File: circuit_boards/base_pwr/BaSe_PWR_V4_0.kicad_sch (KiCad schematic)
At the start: 106 parts, among them J1 12VDC In, J1 USB_C_Receptacle, J10 Conn_01x04_Socket, J11 MOTOR, J3 USB3_A, J3 USB_B_Micro, J4 Conn_01x07_Pin, J5 Conn_02x06_Odd_Even, J7 Conn_02x06_Odd_Even, J7 USB3_B_Micro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

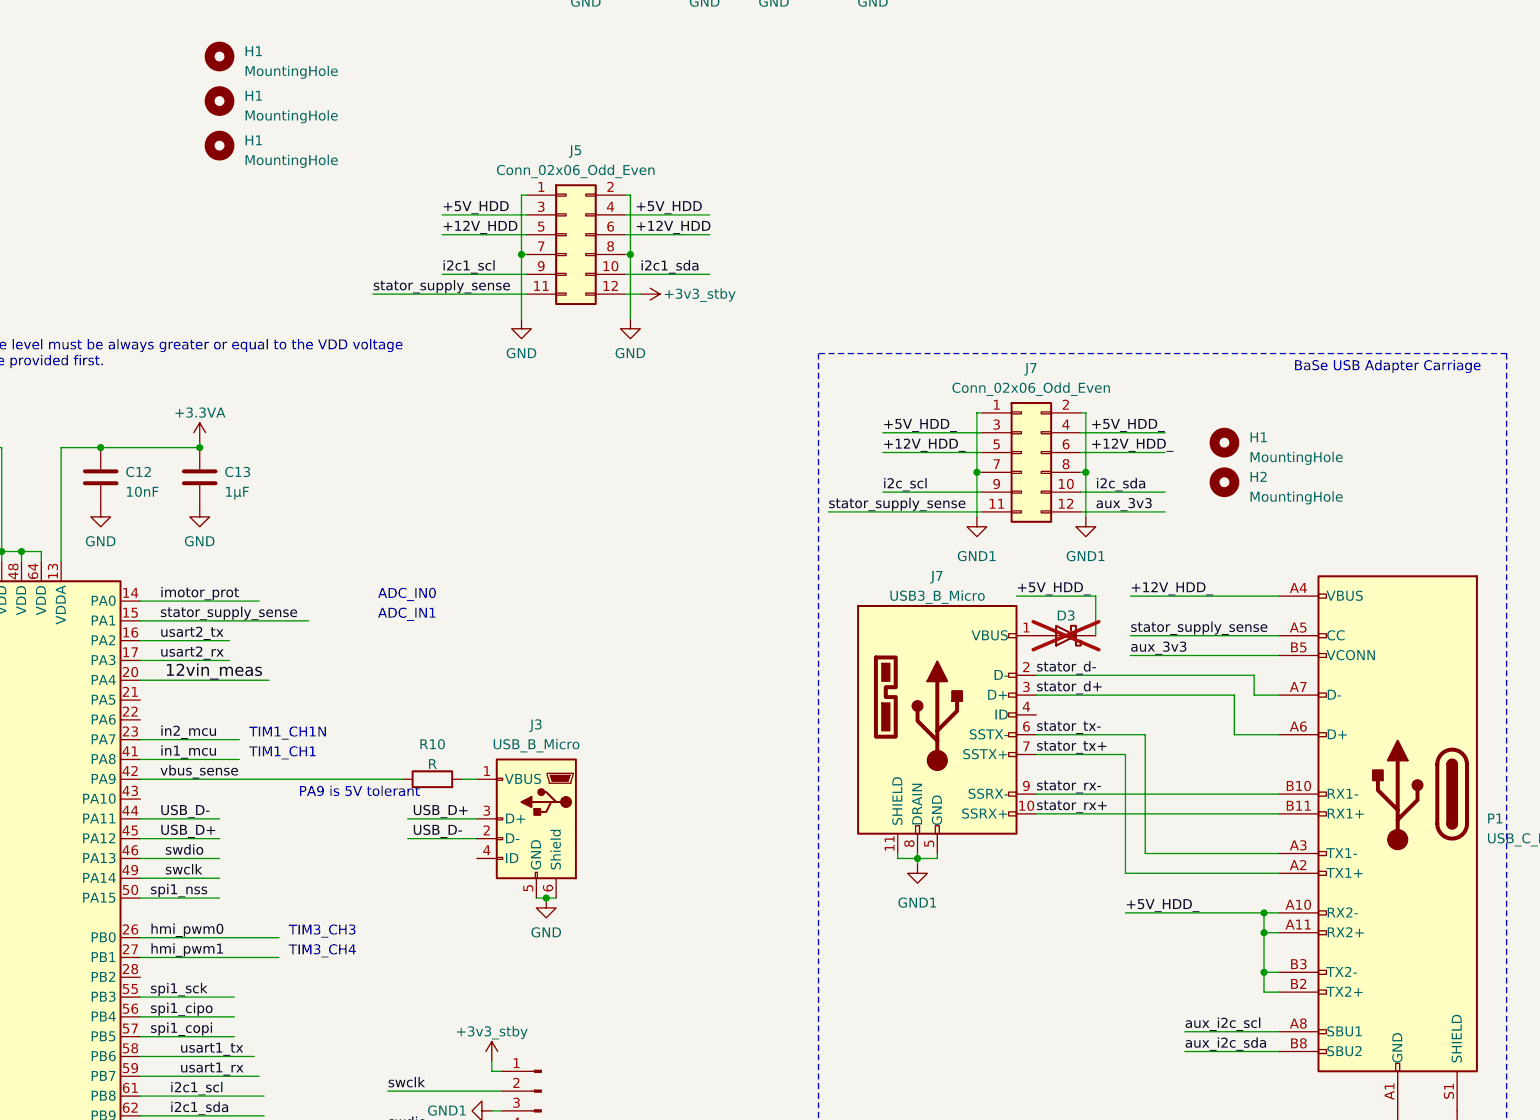
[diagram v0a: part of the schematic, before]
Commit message: BaSe PWR V4.0: add endwitch
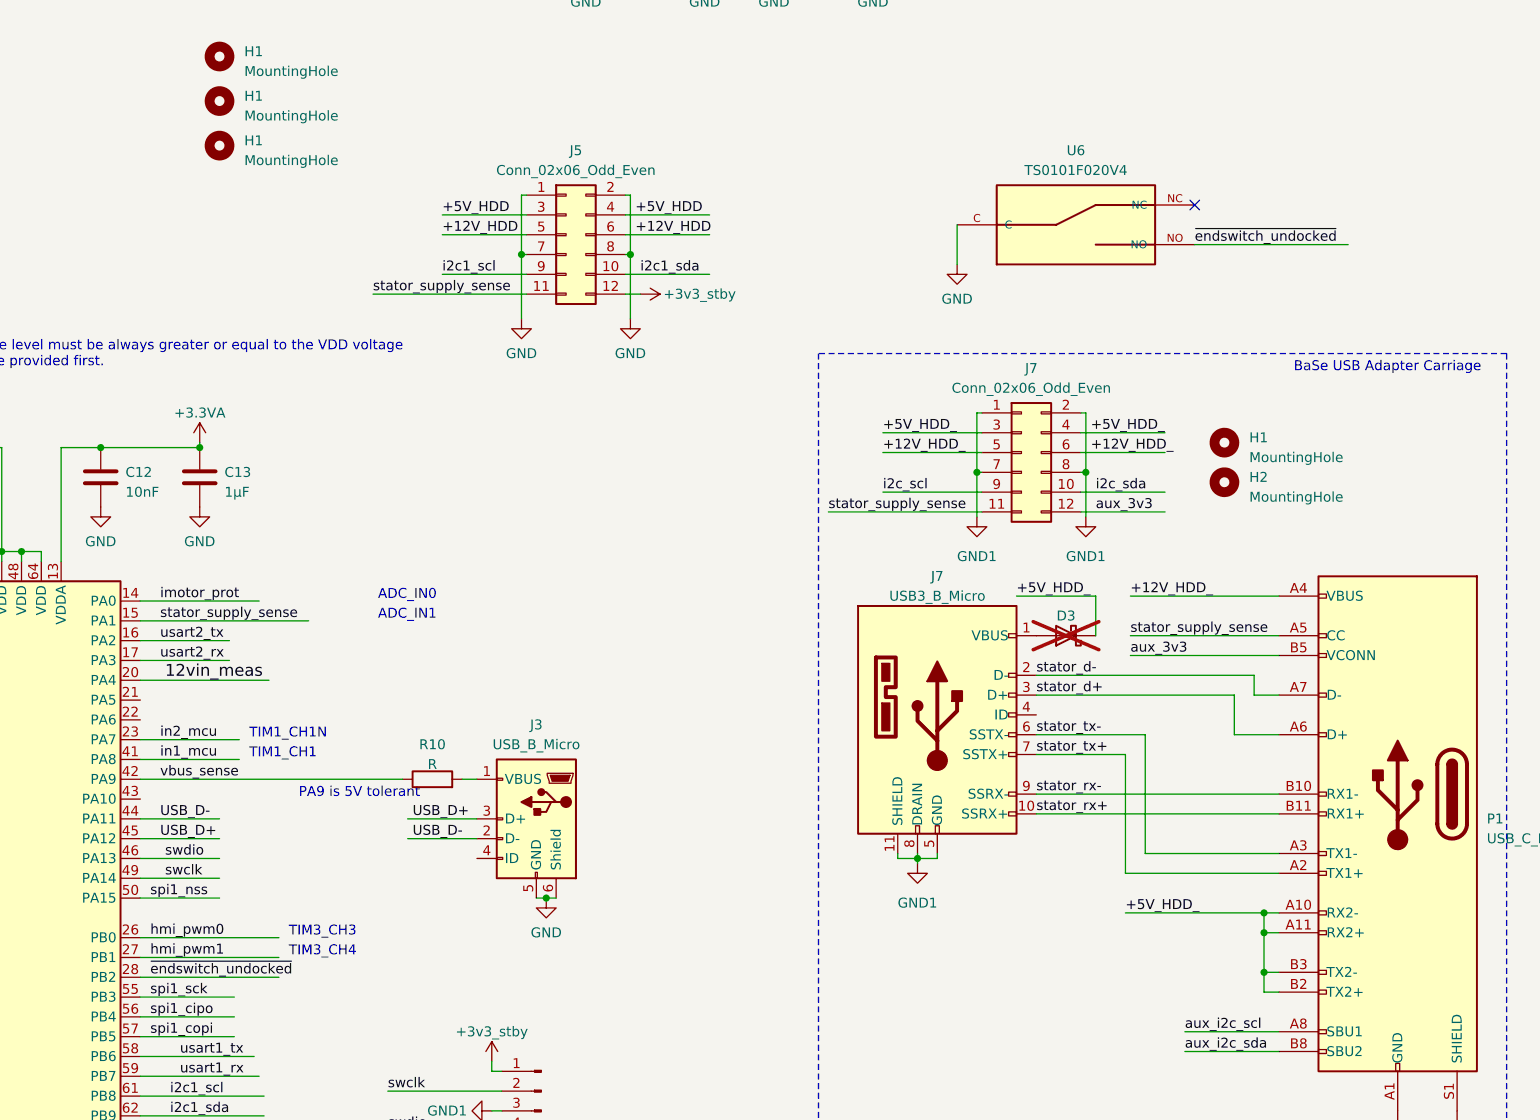
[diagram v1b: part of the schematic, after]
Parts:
- added U6: TS0101F020V4, g7_switch:TS0101F020V4, symbol g7_switch:TS0101F020V4
- BT1: footprint (none) -> Battery:BatteryHolder_Eagle_12BH611-GR; MPN (none) -> 12BH611-GR; Mouser (none) -> 12BH611-GR
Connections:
- net GND: now also U6.C
- net ~{endswitch_undocked}: now reaches U1.28 (PB2)
- net ~{endswitch_undocked}: now also U6.NO
- no-connect marks 8 -> 9
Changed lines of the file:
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@@
   (no_connect (at 328.93 198.12))
   (no_connect (at 328.93 236.22))
+  (no_connect (at 254 127.635))
   (no_connect (at 328.93 193.04))
   (no_connect (at 62.23 129.54))
@@
     (stroke (width 0) (type default))
   )
+  (wire (pts (xy 223.52 130.175) (xy 223.52 135.255))
+    (stroke (width 0) (type default))
+  )
   (wire (pts (xy 38.735 186.055) (xy 41.275 186.055))
     (stroke (width 0) (type default))
@@
     (stroke (width 0) (type default))
   )
+  (wire (pts (xy 254 132.715) (xy 273.685 132.715))
+    (stroke (width 0) (type default))
+  )
   (wire (pts (xy 268.605 77.47) (xy 268.605 76.2))
     (stroke (width 0) (type default))
@@
     (stroke (width 0) (type default))
   )
+  (wire (pts (xy 118.745 226.695) (xy 136.525 226.695))
+    (stroke (width 0) (type default))
+  )
   (wire (pts (xy 29.845 116.84) (xy 62.23 116.84))
     (stroke (width 0) (type default))
@@
     (effects (font (size 1.27 1.27)) (justify left bottom))
   )
+  (label "~{endswitch_undocked}" (at 120.015 226.695 0) (fields_autoplaced)
+    (effects (font (size 1.27 1.27)) (justify left bottom))
+  )
   (label "+12V_HDD_" (at 240.665 159.385 0) (fields_autoplaced)
     (effects (font (size 1.27 1.27)) (justify left bottom))
@@
     (effects (font (size 1.27 1.27)) (justify left bottom))
   )
+  (label "~{endswitch_undocked}" (at 254 132.715 0) (fields_autoplaced)
+    (effects (font (size 1.27 1.27)) (justify left bottom))
+  )
   (label "Dis_DB5" (at 49.53 119.38 0) (fields_autoplaced)
     (effects (font (size 1.524 1.524)) (justify left bottom))
@@
     )
   )
+  (symbol (lib_id "power:GND") (at 223.52 135.255 0) (unit 1)
+    (in_bom yes) (on_board yes) (dnp no) (fields_autoplaced)
+    (property "Reference" "#PWR093" (at 223.52 141.605 0)
+      (effects (font (size 1.27 1.27)) hide)
+    )
+    (property "Value" "GND" (at 223.52 139.7 0)
+      (effects (font (size 1.27 1.27)))
+    )
+    (property "Footprint" "" (at 223.52 135.255 0)
+      (effects (font (size 1.27 1.27)) hide)
+    )
+    (property "Datasheet" "" (at 223.52 135.255 0)
+      (effects (font (size 1.27 1.27)) hide)
+    )
+    (pin "1")
+    (instances
+      (project "BaSe_PWR_V4_0"
+        (path "/e86c76e9-1b7b-4477-86ba-921b1581c6da"
+          (reference "#PWR093") (unit 1)
+        )
+      )
+    )
+  )
   (symbol (lib_id "Waberinator_rev1-rescue:GND") (at 75.565 41.275 0) (unit 1)
     (in_bom yes) (on_board yes) (dnp no)
@@
       (effects (font (size 1.27 1.27)) (justify left))
     )
-    (property "Footprint" "" (at 57.785 57.531 90)
+    (property "Footprint" "Battery:BatteryHolder_Eagle_12BH611-GR" (at 57.785 57.531 90)
+      (effects (font (size 1.27 1.27)) hide)
+    )
+    (property "Datasheet" "https://www.mouser.de/datasheet/2/209/EPD-200766-1274481.pdf" (at 57.785 57.531 90)
       (effects (font (size 1.27 1.27)) hide)
     )
-    (property "Datasheet" "~" (at 57.785 57.531 90)
+    (property "MPN" "12BH611-GR" (at 57.785 59.055 0)
+      (effects (font (size 1.27 1.27)) hide)
+    )
+    (property "Mouser" " 12BH611-GR " (at 57.785 59.055 0)
+      (effects (font (size 1.27 1.27)) hide)
+    )
+    (property "Field6" "" (at 57.785 59.055 0)
       (effects (font (size 1.27 1.27)) hide)
     )
@@
         )
       )
+    )
+  )
+  (symbol (lib_id "g7_switch:TS0101F020V4") (at 238.76 135.255 0) (unit 1)
+    (in_bom yes) (on_board yes) (dnp no) (fields_autoplaced)
+    (property "Reference" "U6" (at 238.76 120.65 0)
+      (effects (font (size 1.27 1.27)))
+    )
+    (property "Value" "TS0101F020V4" (at 238.76 123.19 0)
+      (effects (font (size 1.27 1.27)))
+    )
+    (property "Footprint" "g7_switch:TS0101F020V4" (at 238.76 135.255 0)
+      (effects (font (size 1.27 1.27)) (justify bottom) hide)
+    )
+    (property "Datasheet" "https://sten-eswitch-13110800-production.s3.amazonaws.com/system/asset/product_line/data_sheet/126/TS.pdf" (at 238.76 135.255 0)
+      (effects (font (size 1.27 1.27)) hide)
+    )
+    (property "Digikey" "EG4938-ND" (at 238.76 135.255 0)
+      (effects (font (size 1.27 1.27)) hide)
+    )
+    (pin "C")
+    (pin "NC")
+    (pin "NO")
+    (instances
+      (project "BaSe_PWR_V4_0"
+        (path "/e86c76e9-1b7b-4477-86ba-921b1581c6da"
+          (reference "U6") (unit 1)
+        )
+      )

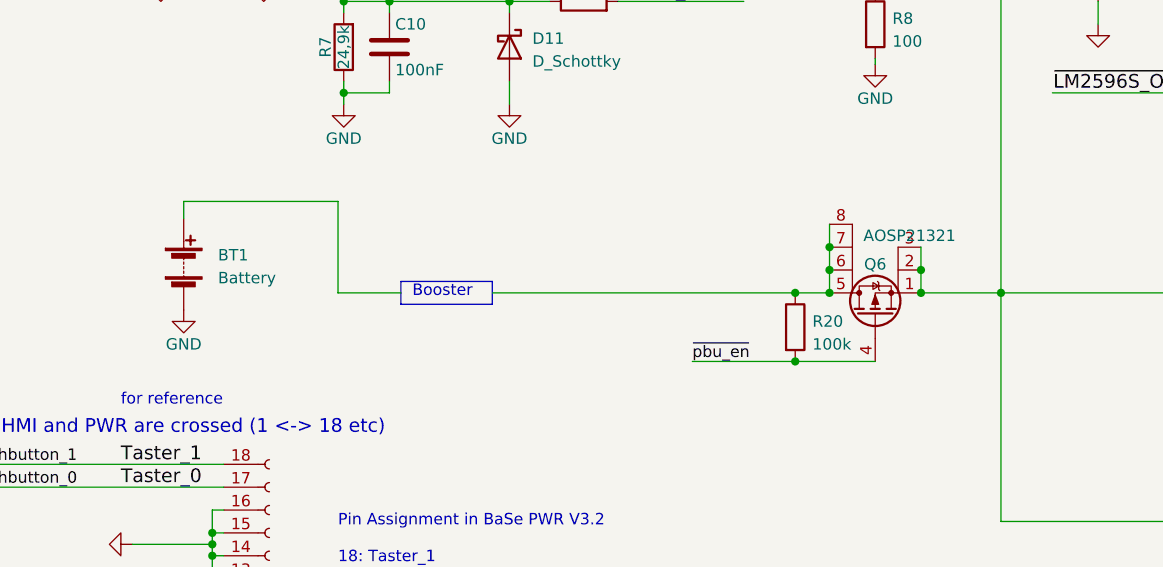
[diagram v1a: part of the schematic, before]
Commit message: BaSe PWR V4.0: add 3d models, define layer stackup
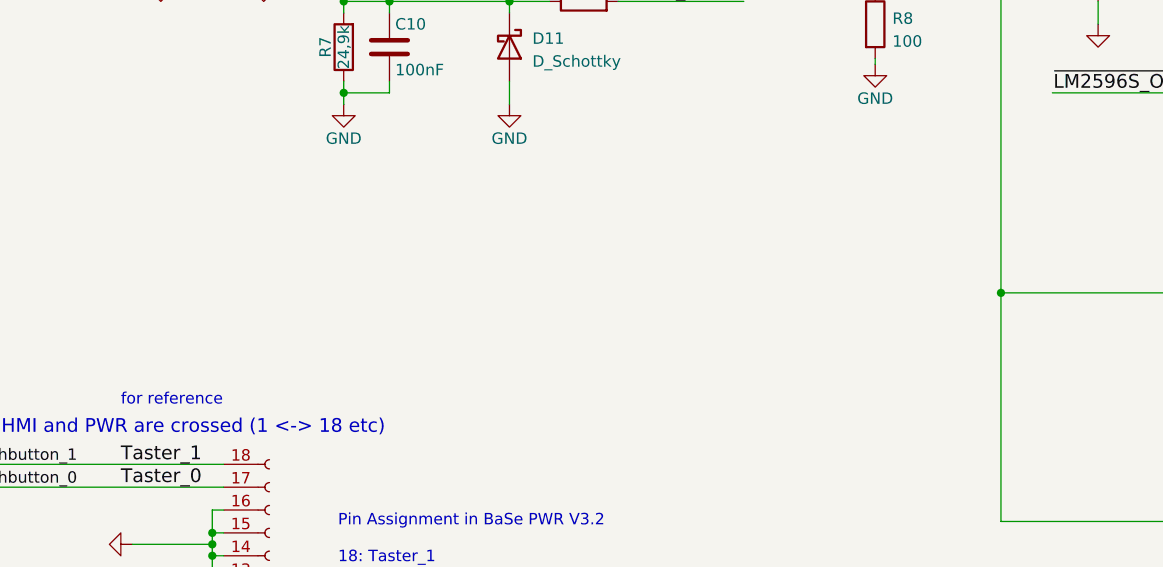
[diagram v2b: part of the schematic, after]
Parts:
- removed BT1: Battery, Battery:BatteryHolder_Eagle_12BH611-GR, symbol Device:Battery
- removed Q6: AOSP21321, Package_SO:SO-8_3.9x4.9mm_P1.27mm, symbol Device:Q_PMOS_DGS
- removed R20: 100k, Resistor_SMD:R_0603_1608Metric_Pad0.98x0.95mm_HandSolder, symbol Device:R
- J3: footprint Connector_USB:USB_Micro-B_Molex-105017-0001 -> g7_connectors:USB_Micro-B_Molex-105017-0001
- L1: footprint Inductor_SMD:L_Wuerth_WE-PD-Typ-LS_Handsoldering -> g7_inductor:L_Wuerth_WE-PD-Typ-LS_Handsoldering
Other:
- note removed: "Booster"

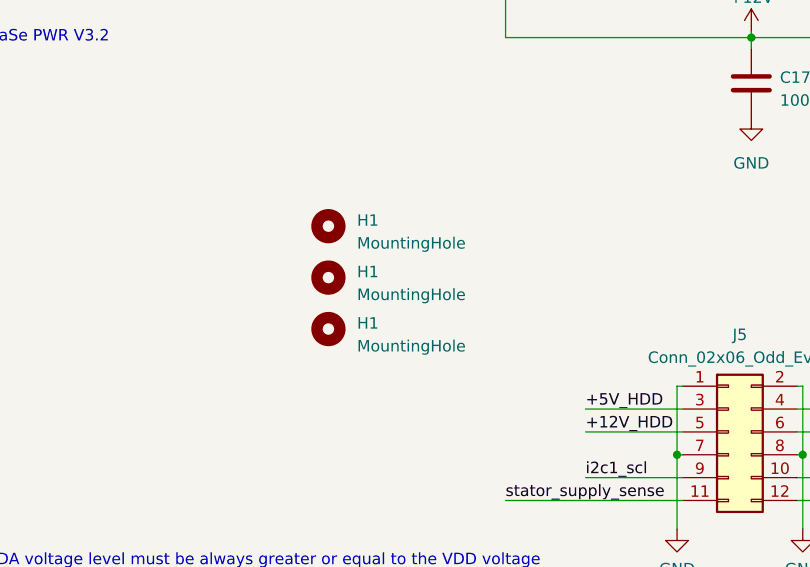
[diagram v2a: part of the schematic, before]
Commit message: BaSe PWR V4.0: push to MCAD. Moved some stuff.
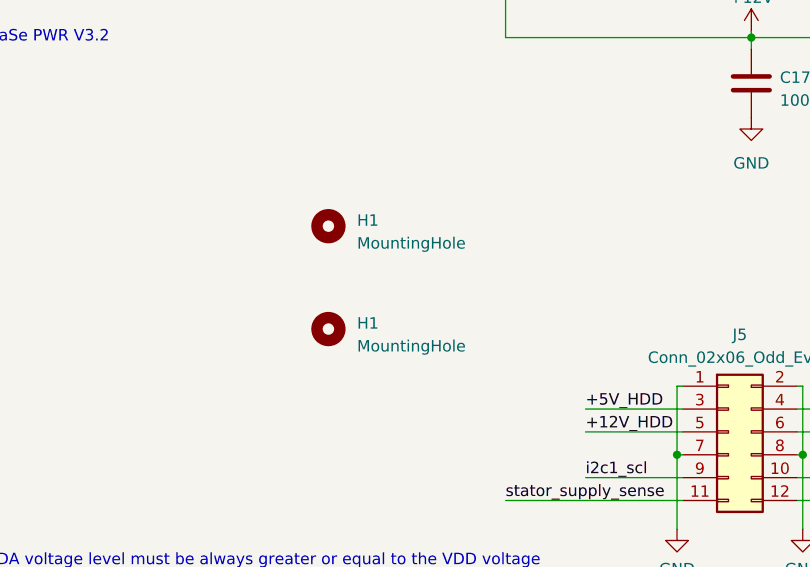
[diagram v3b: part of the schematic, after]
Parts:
- removed H1: MountingHole, MountingHole:MountingHole_2.7mm_M2.5_DIN965, symbol Mechanical:MountingHole
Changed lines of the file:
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@@
-    )
-  )
-  (symbol (lib_id "Mechanical:MountingHole") (at 128.905 114.3 0) (unit 1)
-    (in_bom yes) (on_board yes) (dnp no) (fields_autoplaced)
-    (property "Reference" "H1" (at 132.08 113.665 0)
-      (effects (font (size 1.27 1.27)) (justify left))
-    )
-    (property "Value" "MountingHole" (at 132.08 116.205 0)
-      (effects (font (size 1.27 1.27)) (justify left))
-    )
-    (property "Footprint" "MountingHole:MountingHole_2.7mm_M2.5_DIN965" (at 128.905 114.3 0)
-      (effects (font (size 1.27 1.27)) hide)
-    )
-    (property "Datasheet" "~" (at 128.905 114.3 0)
-      (effects (font (size 1.27 1.27)) hide)
-    )
-    (instances
-      (project "Base_Motor_Test_USB_Adapter_Carriage"
-        (path "/1c5bbc7b-46b4-48d2-afc3-38571a0ba4f9"
-          (reference "H1") (unit 1)
-        )
-      )
-      (project "BaSe_PWR_V4_0"
-        (path "/e86c76e9-1b7b-4477-86ba-921b1581c6da"
-          (reference "H6") (unit 1)
-        )
-      )
     )
   )

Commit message: BaSe PWR V4.0: probably final placement, start routing
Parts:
- added C27: 22µF, Capacitor_THT:C_Radial_D5.0mm_H11.0mm_P2.00mm, symbol Waberinator_rev1-rescue:CP
- added FB2: FerriteBead, Capacitor_SMD:C_1206_3216Metric_Pad1.33x1.80mm_HandSolder, symbol Device:FerriteBead
- J2: footprint Connector_PinHeader_2.54mm:PinHeader_1x18_P2.54mm_Vertical -> Connector_PinHeader_1.27mm:PinHeader_1x18_P1.27mm_Vertical
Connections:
- net +12V: now also FB2.1; no longer C25.1, U5.5 (VM)
- net GND: now also J4.3 (Pin_3), C27.2
- net GND1: no longer J4.3 (Pin_3)
- net stator_supply_sense: no longer J7.11 (Pin_11), P1.A5 (CC)
- net motor1: now reaches J11.1 (Pin_1)
- net motor1: now also U5.6 (OUT1); no longer U5.4 (OUT2)
- net motor2: now reaches J11.2 (Pin_2)
- net motor2: now also U5.4 (OUT2); no longer U5.6 (OUT1)
- new net 12v_motor: C25.1, C27.1, FB2.2, U5.5 (VM)
- new net stator_supply_sense_: J7.11 (Pin_11), P1.A5 (CC)
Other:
- moved on the sheet: C24, J11

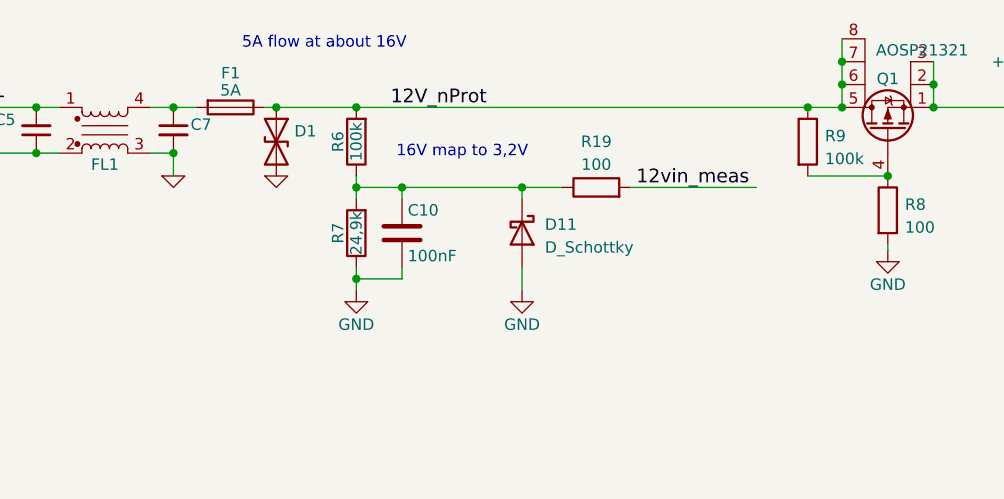
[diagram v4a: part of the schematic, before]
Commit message: BaSe_PWR_V4_0: add gnd planes on outer layers, thicked up DC input tracks to carry 5A
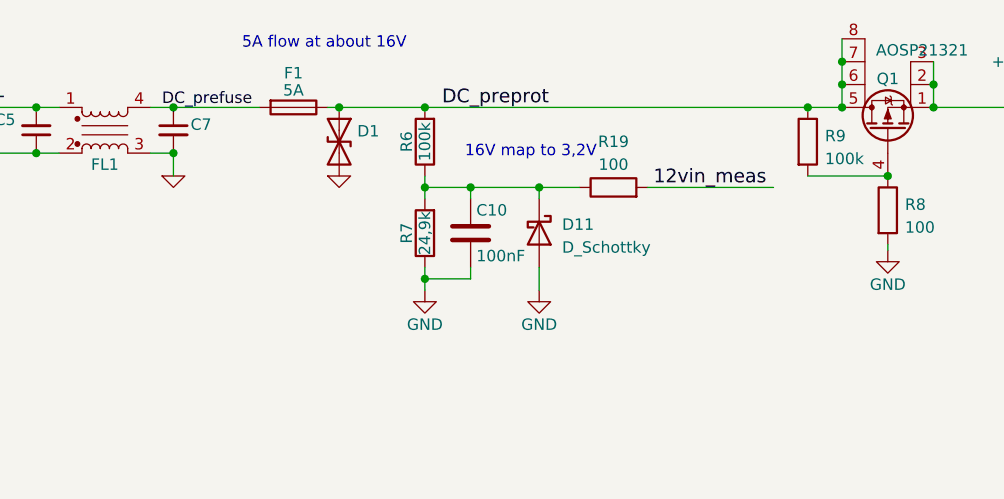
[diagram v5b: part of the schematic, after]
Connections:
- net DC_prefuse: now reaches C7.1, F1.2, FL1.4
- net 12V_nProt renamed DC_preprot
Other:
- moved on the sheet: C10, D1, D11, F1, R19, R6, R7
